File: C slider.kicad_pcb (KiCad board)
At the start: 2 copper layers, 50 x 36 mm, 11 parts, among them J1 Conn_01x04_Pin, J2 Conn_01x02_Pin, U3 ATtiny412-SS

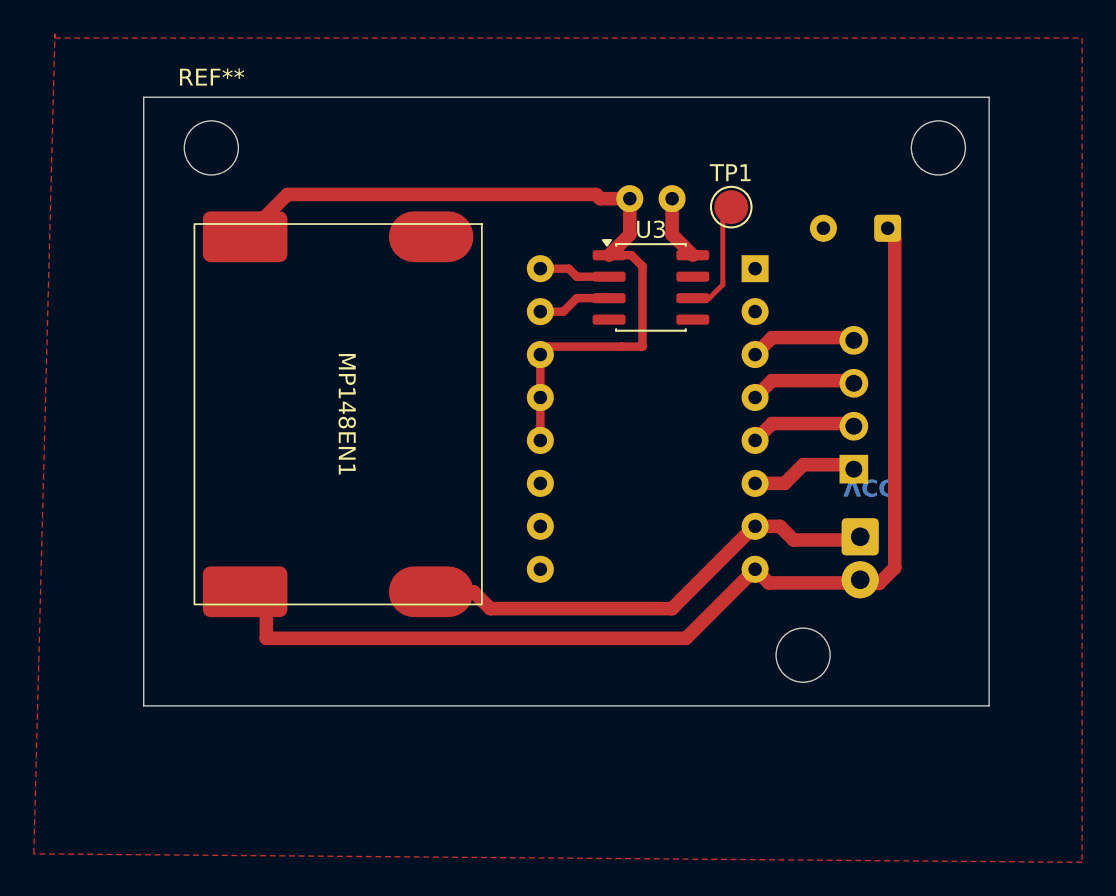
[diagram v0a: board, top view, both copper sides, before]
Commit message: pridani svorkovnice, uprava GND a tras na attiny
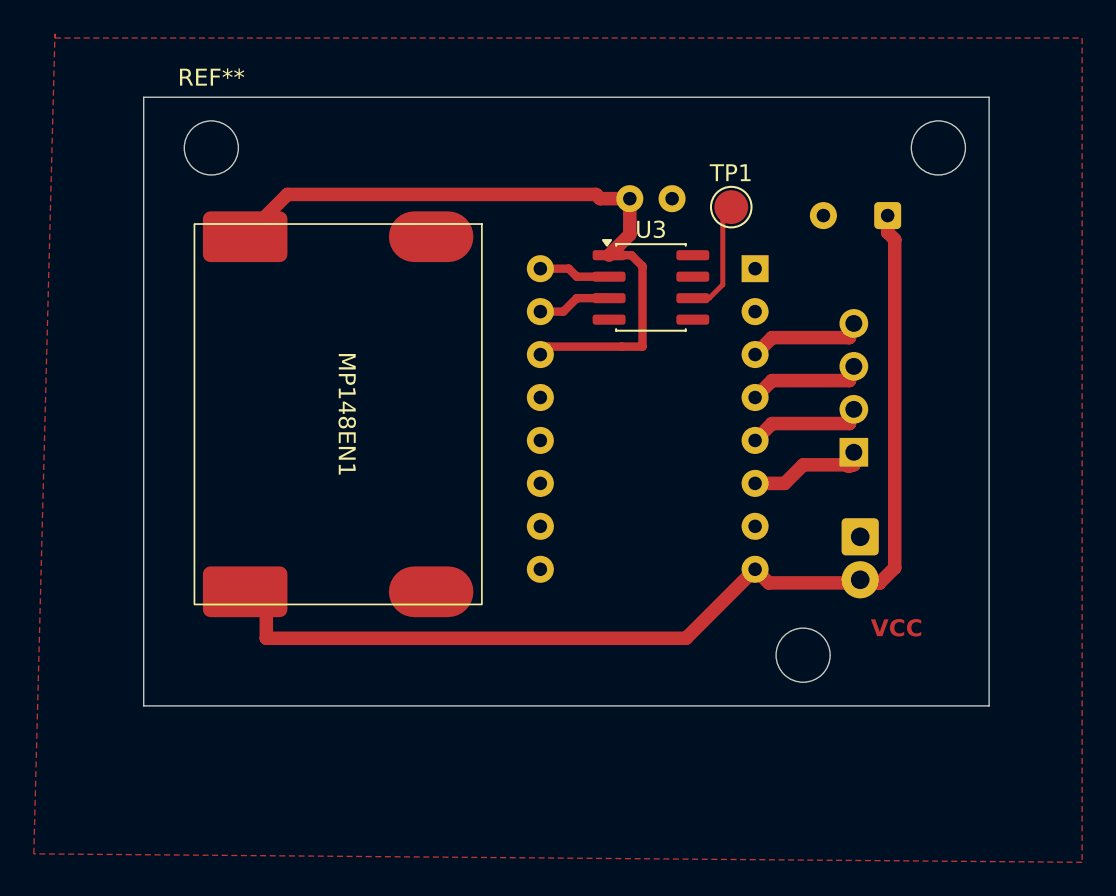
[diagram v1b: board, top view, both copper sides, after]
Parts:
- moved J1 1.00 mm to (143.0, 115.0)
- moved C1 0.75 mm to (145.0, 101.0)
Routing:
- net GND: track 32.0 -> 0.04 mm
- net Net-(A1-M2): track 46.7 -> 41.7 mm
- net +12V: track 63.1 -> 63.9 mm
